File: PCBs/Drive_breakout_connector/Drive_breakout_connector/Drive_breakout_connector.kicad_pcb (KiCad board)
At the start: 2 copper layers, 24 x 10 mm, 4 parts, among them J1 Socket, J2 JST_GH Input

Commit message: arm, drive and power modifications
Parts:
- moved H1 0.24 mm to (80.5, 50.5)
- moved H2 0.15 mm to (99.2, 50.5)
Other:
- outline, holes or cut-outs redrawn
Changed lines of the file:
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@@
 	(footprint "MountingHole:MountingHole_2.7mm_M2.5_DIN965_Pad"
 		(layer "F.Cu")
-		(at 80.5 50.25)
+		(at 80.5 50.495)
 		(descr "Mounting Hole 2.7mm, M2.5, DIN965")
 		(tags "mounting hole 2.7mm m2.5 din965")
@@
 	(footprint "MountingHole:MountingHole_2.7mm_M2.5_DIN965_Pad"
 		(layer "F.Cu")
-		(at 99 50.46)
+		(at 99.15 50.495)
 		(descr "Mounting Hole 2.7mm, M2.5, DIN965")
 		(tags "mounting hole 2.7mm m2.5 din965")
@@
 		)
 	)
-	(gr_rect
+	(gr_line
 		(start 77.75 45.495)
-		(end 101.75 55.495)
+		(end 77.75 55.495)
 		(stroke
 			(width 0.05)
-			(type solid)
-		)
-		(fill no)
+			(type default)
+		)
 		(layer "Edge.Cuts")
 	)
+	(gr_line
+		(start 101.75 55.495)
+		(end 77.75 55.495)
+		(stroke
+			(width 0.05)
+			(type default)
+		)
+		(layer "Edge.Cuts")
+	)
+	(gr_line
+		(start 96.75 45.495)
+		(end 77.75 45.495)
+		(stroke
+			(width 0.05)
+			(type default)
+		)
+		(layer "Edge.Cuts")
+	)
+	(dimension
+		(type orthogonal)
+		(layer "Edge.Cuts")
+		(pts
+			(xy 99.15 50.495) (xy 101.75 45.495)
+		)
+		(height 9.5)
+		(orientation 1)
+		(format
+			(prefix "")
+			(suffix "")
+			(units 3)
+			(units_format 0)
+			(precision 4)
+			(suppress_zeroes yes)
+		)
+		(style
+			(thickness 0.05)
+			(arrow_length 1.27)
+			(text_position_mode 0)
+			(arrow_direction outward)
+			(extension_height 0.58642)
+			(extension_offset 0.5)
+			(keep_text_aligned yes)
+		)
+		(gr_text "5"
+			(at 107.5 47.995 90)
+			(layer "Edge.Cuts")
+			(effects
+				(font
+					(size 1 1)
+					(thickness 0.15)
+				)
+			)
+		)
+	)
+	(dimension
+		(type orthogonal)
+		(layer "Edge.Cuts")
+		(pts
+			(xy 101.75 45.495) (xy 96.75 45.495)
+		)
+		(height -2.815)
+		(orientation 0)
+		(format
+			(prefix "")
+			(suffix "")
+			(units 3)
+			(units_format 0)
+			(precision 4)
+			(suppress_zeroes yes)
+		)
+		(style
+			(thickness 0.05)
+			(arrow_length 1.27)
+			(text_position_mode 0)
+			(arrow_direction outward)
+			(extension_height 0.58642)
+			(extension_offset 0.5)
+			(keep_text_aligned yes)
+		)
+		(gr_text "5"
+			(at 99.25 41.53 0)
+			(layer "Edge.Cuts")
+			(effects
+				(font
+					(size 1 1)
+					(thickness 0.15)
+				)
+			)
+		)
+	)
 	(segment

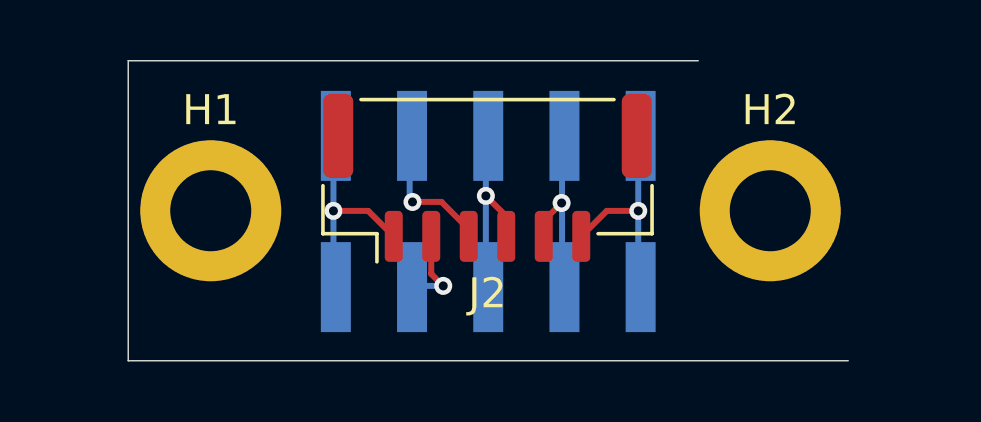
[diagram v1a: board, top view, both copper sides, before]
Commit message: rounded boards David, someone could cut themselves otherwise
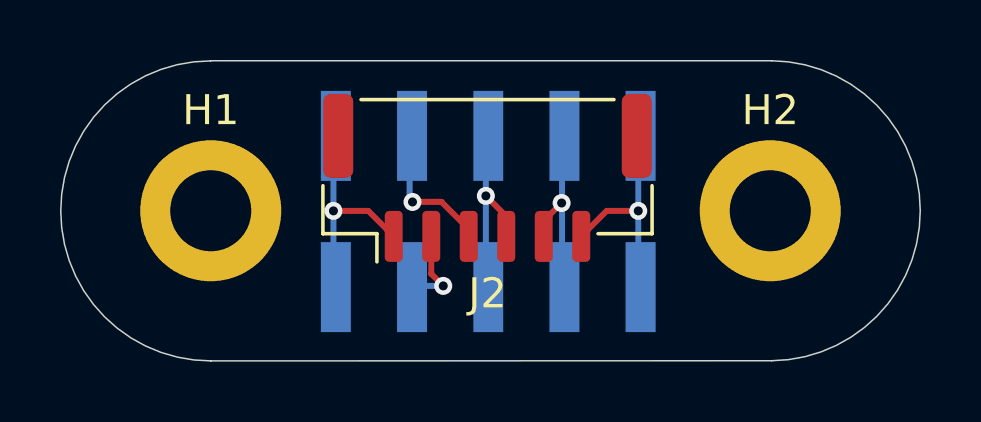
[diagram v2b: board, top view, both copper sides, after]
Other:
- board size 24 x 10 mm -> 28.7 x 10 mm
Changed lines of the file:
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@@
 		)
 	)
+	(gr_arc
+		(start 80.5 55.5)
+		(mid 75.5 50.5)
+		(end 80.5 45.5)
+		(stroke
+			(width 0.05)
+			(type solid)
+		)
+		(layer "Edge.Cuts")
+	)
 	(gr_line
-		(start 77.75 45.495)
-		(end 77.75 55.495)
+		(start 99.1999 55.495)
+		(end 80.5 55.5)
 		(stroke
 			(width 0.05)
@@
 		(layer "Edge.Cuts")
 	)
-	(gr_line
-		(start 101.75 55.495)
-		(end 77.75 55.495)
+	(gr_arc
+		(start 99.201072 45.495012)
+		(mid 104.150249 50.495586)
+		(end 99.1999 55.495)
 		(stroke
 			(width 0.05)
-			(type default)
+			(type solid)
 		)
 		(layer "Edge.Cuts")
 	)
 	(gr_line
-		(start 96.75 45.495)
-		(end 77.75 45.495)
+		(start 99.201072 45.495012)
+		(end 80.5 45.495002)
 		(stroke
 			(width 0.05)
